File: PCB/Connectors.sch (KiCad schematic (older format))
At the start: 16 parts, among them J1 S2B-PH-SM4-TB, J10 DNP, J11 DNP, J12 DNP, J13 DNP, J2 TRANSDUCER, J3 DNP, J4 PH1-08-UA, J5 DNP, J6 DNP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

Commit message: Rearrange FPGA connections, combine VGA and ADC debug headers, layout most of VGA and ADC circuits
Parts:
- removed J10: DNP, Pin_Headers:Pin_Header_Straight_1x05_Pitch2.54mm, symbol Connector:Conn_01x05_Male
- removed J8: DNP, Pin_Headers:Pin_Header_Straight_1x03_Pitch2.54mm, symbol Connector:Conn_01x03_Male
- added J8: PH1-08-UA, Pin_Headers:Pin_Header_Straight_1x08_Pitch2.54mm, symbol Connector:Conn_01x08_Male
- renumbered J11 to J10, J12 to J11, J13 to J12
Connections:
- net ADC-SCK: now also J8.6 (Pin_6)
- net ADC-SDO: now also J8.7 (Pin_7)
- net ADC-~CS: now also J8.8 (Pin_8)
- net VGA-D0: now also J8.2 (Pin_2)
- net VGA-D1: now also J8.5 (Pin_5)
- net VGA-SCK: now also J8.3 (Pin_3)
- net VGA-~CS0: now also J8.1 (Pin_1)
- net VGA-~CS1: now also J8.4 (Pin_4)
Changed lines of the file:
@@
 	1    0    0    -1
-$EndComp
-$Comp
-L Connector:Conn_01x08_Male J4
-U 1 1 5DD08B5F
-P 3000 4200
-F 0 "J4" H 2972 4174 50  0000 R CNN
-F 1 "PH1-08-UA" H 2972 4083 50  0000 R CNN
-F 2 "Pin_Headers:Pin_Header_Straight_1x08_Pitch2.54mm" H 3000 4200 50  0001 C CNN
-F 3 "https://www.digikey.ca/product-detail/en/adam-tech/PH1-08-UA/2057-PH1-08-UA-ND/9830442" H 3000 4200 50  0001 C CNN
-	1    3000 4200
-	-1   0    0    -1
 $EndComp
 Text GLabel 2750 4000 0    50   Input ~ 0
@@
 $EndComp
 $Comp
-L Connector:Conn_01x02_Male J12
+L Connector:Conn_01x02_Male J11
 U 1 1 5DED5F02
 P 6500 5950
-F 0 "J12" H 6472 5832 50  0000 R CNN
+F 0 "J11" H 6472 5832 50  0000 R CNN
 F 1 "DNP" H 6472 5923 50  0000 R CNN
 F 2 "Pin_Headers:Pin_Header_Straight_1x02_Pitch2.54mm" H 6500 5950 50  0001 C CNN
@@
 Text GLabel 8800 4900 0    50   Input ~ 0
 ADC-SDO
-Text GLabel 8800 5600 0    50   Input ~ 0
+Text GLabel 8800 5500 0    50   Input ~ 0
 VGA-~CS0
-Text GLabel 8800 5500 0    50   Input ~ 0
+Text GLabel 8800 5400 0    50   Input ~ 0
 VGA-D0
-Text GLabel 8800 5400 0    50   Input ~ 0
+Text GLabel 8800 5300 0    50   Input ~ 0
 VGA-SCK
+Text GLabel 8800 5100 0    50   Input ~ 0
+VGA-D1
 Text GLabel 8800 5200 0    50   Input ~ 0
-VGA-D1
-Text GLabel 8800 5300 0    50   Input ~ 0
 VGA-~CS1
 Text GLabel 8800 6100 0    50   Input ~ 0
@@
 Wire Wire Line
 	8800 4600 8850 4600
-$Comp
-L Connector:Conn_01x03_Male J8
-U 1 1 5E22DC4D
-P 9050 4900
-F 0 "J8" H 9022 4832 50  0000 R CNN
-F 1 "DNP" H 9022 4923 50  0000 R CNN
-F 2 "Pin_Headers:Pin_Header_Straight_1x03_Pitch2.54mm" H 9050 4900 50  0001 C CNN
-F 3 "~" H 9050 4900 50  0001 C CNN
-	1    9050 4900
-	-1   0    0    1
-$EndComp
 Wire Wire Line
 	8800 4800 8850 4800
@@
 	8800 5000 8850 5000
 Wire Wire Line
+	8800 5100 8850 5100
+Wire Wire Line
 	8800 5200 8850 5200
 Wire Wire Line
@@
 	8800 5400 8850 5400
 Wire Wire Line
-	8800 5500 8850 5500
-Wire Wire Line
-	8850 5600 8800 5600
+	8850 5500 8800 5500
 Wire Wire Line
 	8800 5800 8850 5800
@@
 $EndComp
 $Comp
-L Connector_Generic:Conn_02x05_Odd_Even J11
+L Connector_Generic:Conn_02x05_Odd_Even J10
 U 1 1 5E09FA0E
 P 2750 5750
-F 0 "J11" H 2800 6167 50  0000 C CNN
+F 0 "J10" H 2800 6167 50  0000 C CNN
 F 1 "DNP" H 2800 6076 50  0000 C CNN
 F 2 "Pin_Headers:Pin_Header_Straight_2x05_Pitch2.54mm" H 2750 5750 50  0001 C CNN
@@
 NoConn ~ 2550 5850
 $Comp
-L Connector:Conn_01x04_Male J13
+L Connector:Conn_01x04_Male J12
 U 1 1 5E5FD68B
 P 9050 6000
-F 0 "J13" H 9022 5882 50  0000 R CNN
+F 0 "J12" H 9022 5882 50  0000 R CNN
 F 1 "DNP" H 9022 5973 50  0000 R CNN
 F 2 "Pin_Headers:Pin_Header_Straight_1x04_Pitch2.54mm" H 9050 6000 50  0001 C CNN
 F 3 "~" H 9050 6000 50  0001 C CNN
 	1    9050 6000
-	-1   0    0    1
-$EndComp
-$Comp
-L Connector:Conn_01x05_Male J10
-U 1 1 5E600171
-P 9050 5400
-F 0 "J10" H 9022 5332 50  0000 R CNN
-F 1 "DNP" H 9022 5423 50  0000 R CNN
-F 2 "Pin_Headers:Pin_Header_Straight_1x05_Pitch2.54mm" H 9050 5400 50  0001 C CNN
-F 3 "~" H 9050 5400 50  0001 C CNN
-	1    9050 5400
 	-1   0    0    1
 $EndComp
@@
 	-1   0    0    -1
 $EndComp
+$Comp
+L Connector:Conn_01x08_Male J4
+U 1 1 5DD08B5F
+P 3000 4200
+F 0 "J4" H 2972 4174 50  0000 R CNN
+F 1 "PH1-08-UA" H 2972 4083 50  0000 R CNN
+F 2 "Pin_Headers:Pin_Header_Straight_1x08_Pitch2.54mm" H 3000 4200 50  0001 C CNN
+F 3 "https://www.digikey.ca/product-detail/en/adam-tech/PH1-08-UA/2057-PH1-08-UA-ND/9830442" H 3000 4200 50  0001 C CNN
+	1    3000 4200
+	-1   0    0    -1
+$EndComp
+$Comp
+L Connector:Conn_01x08_Male J8
+U 1 1 5E2E1494
+P 9050 5200
+F 0 "J8" H 9022 5174 50  0000 R CNN
+F 1 "PH1-08-UA" H 9022 5083 50  0000 R CNN
+F 2 "Pin_Headers:Pin_Header_Straight_1x08_Pitch2.54mm" H 9050 5200 50  0001 C CNN
+F 3 "https://www.digikey.ca/product-detail/en/adam-tech/PH1-08-UA/2057-PH1-08-UA-ND/9830442" H 9050 5200 50  0001 C CNN
+	1    9050 5200
+	-1   0    0    1
+$EndComp
 $EndSCHEMATC

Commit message: Add additional mounting holes, optimize receive power supply connections for layout, simplify FPGA analog ground, layout 3v3 and 1v2 supplies
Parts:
- added H3, H4: MountingHole_Pad, Mounting_Holes:MountingHole_4mm_Pad_Via, symbol Mechanical:MountingHole_Pad
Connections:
- net GND: now also H3.1, H4.1
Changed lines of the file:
@@
 $EndDescr
 $Comp
-L power:GND #PWR0179
+L power:GND #PWR0178
 U 1 1 5DCE40E5
 P 2750 2200
-F 0 "#PWR0179" H 2750 1950 50  0001 C CNN
+F 0 "#PWR0178" H 2750 1950 50  0001 C CNN
 F 1 "GND" H 2755 2027 50  0000 C CNN
 F 2 "" H 2750 2200 50  0001 C CNN
@@
 $EndComp
 $Comp
-L power:+BATT #PWR0177
+L power:+BATT #PWR0176
 U 1 1 5DCED91D
 P 3000 2000
-F 0 "#PWR0177" H 3000 1850 50  0001 C CNN
+F 0 "#PWR0176" H 3000 1850 50  0001 C CNN
 F 1 "+BATT" H 3015 2173 50  0000 C CNN
 F 2 "" H 3000 2000 50  0001 C CNN
@@
 	5700 2550 5700 2650
 $Comp
-L power:GND #PWR0181
+L power:GND #PWR0182
 U 1 1 5DE80E0C
 P 5700 3050
-F 0 "#PWR0181" H 5700 2800 50  0001 C CNN
+F 0 "#PWR0182" H 5700 2800 50  0001 C CNN
 F 1 "GND" H 5705 2877 50  0000 C CNN
 F 2 "" H 5700 3050 50  0001 C CNN
@@
 FPGA-TDO
 $Comp
-L power:+3V3 #PWR0182
+L power:+3V3 #PWR0183
 U 1 1 5DED008E
 P 2700 3900
-F 0 "#PWR0182" H 2700 3750 50  0001 C CNN
+F 0 "#PWR0183" H 2700 3750 50  0001 C CNN
 F 1 "+3V3" H 2715 4073 50  0000 C CNN
 F 2 "" H 2700 3900 50  0001 C CNN
@@
 	2800 4600 2750 4600
 $Comp
-L power:GND #PWR0185
+L power:GND #PWR0186
 U 1 1 5DD2AB1C
 P 2050 4450
-F 0 "#PWR0185" H 2050 4200 50  0001 C CNN
+F 0 "#PWR0186" H 2050 4200 50  0001 C CNN
 F 1 "GND" H 2055 4277 50  0000 C CNN
 F 2 "" H 2050 4450 50  0001 C CNN
@@
 Connection ~ 2050 4400
 $Comp
-L power:GND #PWR0193
+L power:GND #PWR0194
 U 1 1 5DD3A2BB
 P 3150 6000
-F 0 "#PWR0193" H 3150 5750 50  0001 C CNN
+F 0 "#PWR0194" H 3150 5750 50  0001 C CNN
 F 1 "GND" H 3155 5827 50  0000 C CNN
 F 2 "" H 3150 6000 50  0001 C CNN
@@
 	5950 2650 5950 3000
 $Comp
-L power:+2V5 #PWR0190
+L power:+2V5 #PWR0191
 U 1 1 5DDAEE31
 P 3250 5650
-F 0 "#PWR0190" H 3250 5500 50  0001 C CNN
+F 0 "#PWR0191" H 3250 5500 50  0001 C CNN
 F 1 "+2V5" H 3265 5823 50  0000 C CNN
 F 2 "" H 3250 5650 50  0001 C CNN
@@
 $EndComp
 $Comp
-L power:+1V2 #PWR0183
+L power:+1V2 #PWR0184
 U 1 1 5DECE3B1
 P 6200 3900
-F 0 "#PWR0183" H 6200 3750 50  0001 C CNN
+F 0 "#PWR0184" H 6200 3750 50  0001 C CNN
 F 1 "+1V2" H 6215 4073 50  0000 C CNN
 F 2 "" H 6200 3900 50  0001 C CNN
@@
 	6200 3900 6300 3900
 $Comp
-L power:GND #PWR0184
+L power:GND #PWR0185
 U 1 1 5DECF8CC
 P 6200 4000
-F 0 "#PWR0184" H 6200 3750 50  0001 C CNN
+F 0 "#PWR0185" H 6200 3750 50  0001 C CNN
 F 1 "GND" H 6205 3827 50  0000 C CNN
 F 2 "" H 6200 4000 50  0001 C CNN
@@
 	6200 5200 6300 5200
 $Comp
-L power:GND #PWR0189
+L power:GND #PWR0190
 U 1 1 5DED29DD
 P 6200 5300
-F 0 "#PWR0189" H 6200 5050 50  0001 C CNN
+F 0 "#PWR0190" H 6200 5050 50  0001 C CNN
 F 1 "GND" H 6205 5127 50  0000 C CNN
 F 2 "" H 6200 5300 50  0001 C CNN
@@
 	6200 5300 6300 5300
 $Comp
-L power:+12V #PWR0188
+L power:+12V #PWR0189
 U 1 1 5DED51C9
 P 6200 5200
-F 0 "#PWR0188" H 6200 5050 50  0001 C CNN
+F 0 "#PWR0189" H 6200 5050 50  0001 C CNN
 F 1 "+12V" H 6215 5373 50  0000 C CNN
 F 2 "" H 6200 5200 50  0001 C CNN
@@
 	6200 5850 6300 5850
 $Comp
-L power:GND #PWR0192
+L power:GND #PWR0193
 U 1 1 5DED5F0D
 P 6200 5950
-F 0 "#PWR0192" H 6200 5700 50  0001 C CNN
+F 0 "#PWR0193" H 6200 5700 50  0001 C CNN
 F 1 "GND" H 6205 5777 50  0000 C CNN
 F 2 "" H 6200 5950 50  0001 C CNN
@@
 	6200 5950 6300 5950
 $Comp
-L Parts:+50V #PWR0191
+L Parts:+50V #PWR0192
 U 1 1 5DED7ED3
 P 6200 5850
-F 0 "#PWR0191" H 6200 5700 50  0001 C CNN
+F 0 "#PWR0192" H 6200 5700 50  0001 C CNN
 F 1 "+50V" H 6215 6023 50  0000 C CNN
 F 2 "" H 6200 5850 50  0001 C CNN
@@
 $EndComp
 $Comp
-L power:GND #PWR0187
+L power:GND #PWR0188
 U 1 1 5DEFAC45
 P 6200 4650
-F 0 "#PWR0187" H 6200 4400 50  0001 C CNN
+F 0 "#PWR0188" H 6200 4400 50  0001 C CNN
 F 1 "GND" H 6205 4477 50  0000 C CNN
 F 2 "" H 6200 4650 50  0001 C CNN
@@
 $EndComp
 $Comp
-L power:GND #PWR0180
+L power:GND #PWR0179
 U 1 1 5E243B36
 P 3550 2250
-F 0 "#PWR0180" H 3550 2000 50  0001 C CNN
+F 0 "#PWR0179" H 3550 2000 50  0001 C CNN
 F 1 "GND" H 3555 2077 50  0000 C CNN
 F 2 "" H 3550 2250 50  0001 C CNN
@@
 $EndComp
 $Comp
-L power:+BATT #PWR0178
+L power:+BATT #PWR0177
 U 1 1 5E24725E
 P 3550 2000
-F 0 "#PWR0178" H 3550 1850 50  0001 C CNN
+F 0 "#PWR0177" H 3550 1850 50  0001 C CNN
 F 1 "+BATT" H 3565 2173 50  0000 C CNN
 F 2 "" H 3550 2000 50  0001 C CNN
@@
 	3550 2000 3650 2000
 $Comp
-L power:+10V #PWR0186
+L power:+10V #PWR0187
 U 1 1 5E281EB9
 P 6200 4550
-F 0 "#PWR0186" H 6200 4400 50  0001 C CNN
+F 0 "#PWR0187" H 6200 4400 50  0001 C CNN
 F 1 "+10V" H 6215 4723 50  0000 C CNN
 F 2 "" H 6200 4550 50  0001 C CNN
@@
 	-1   0    0    1
 $EndComp
+$Comp
+L Mechanical:MountingHole_Pad H3
+U 1 1 5E3FBDE7
+P 3750 2500
+F 0 "H3" V 3704 2650 50  0000 L CNN
+F 1 "MountingHole_Pad" V 3795 2650 50  0000 L CNN
+F 2 "Mounting_Holes:MountingHole_4mm_Pad_Via" H 3750 2500 50  0001 C CNN
+F 3 "~" H 3750 2500 50  0001 C CNN
+	1    3750 2500
+	0    1    1    0
+$EndComp
+$Comp
+L power:GND #PWR0180
+U 1 1 5E3FBDF1
+P 3550 2500
+F 0 "#PWR0180" H 3550 2250 50  0001 C CNN
+F 1 "GND" H 3555 2327 50  0000 C CNN
+F 2 "" H 3550 2500 50  0001 C CNN
+F 3 "" H 3550 2500 50  0001 C CNN
+	1    3550 2500
+	1    0    0    -1
+$EndComp
+Wire Wire Line
+	3550 2500 3650 2500
+$Comp
+L Mechanical:MountingHole_Pad H4
+U 1 1 5E3FEDB8
+P 3750 2750
+F 0 "H4" V 3704 2900 50  0000 L CNN
+F 1 "MountingHole_Pad" V 3795 2900 50  0000 L CNN
+F 2 "Mounting_Holes:MountingHole_4mm_Pad_Via" H 3750 2750 50  0001 C CNN
+F 3 "~" H 3750 2750 50  0001 C CNN
+	1    3750 2750
+	0    1    1    0
+$EndComp
+$Comp
+L power:GND #PWR0181
+U 1 1 5E3FEDC2
+P 3550 2750
+F 0 "#PWR0181" H 3550 2500 50  0001 C CNN
+F 1 "GND" H 3555 2577 50  0000 C CNN
+F 2 "" H 3550 2750 50  0001 C CNN
+F 3 "" H 3550 2750 50  0001 C CNN
+	1    3550 2750
+	1    0    0    -1
+$EndComp
+Wire Wire Line
+	3550 2750 3650 2750
 $EndSCHEMATC

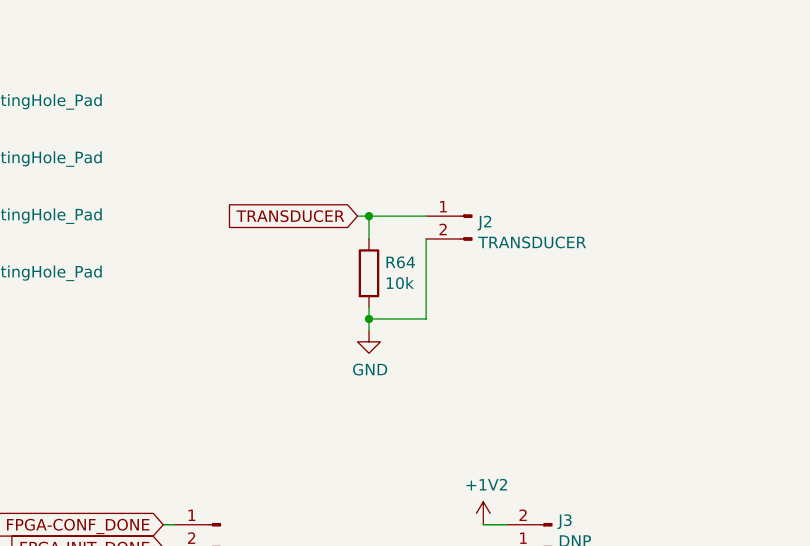
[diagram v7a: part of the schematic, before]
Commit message: Adjust receive circuit to increase stability (hopefully less likely to oscillate)
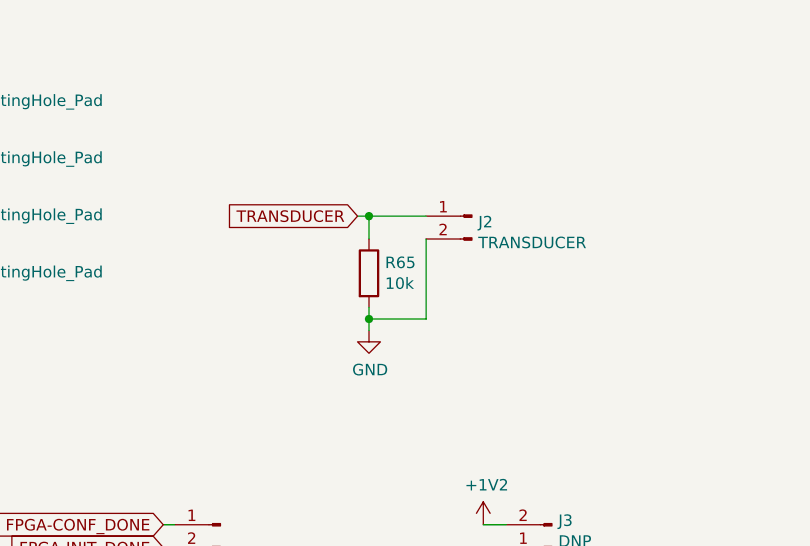
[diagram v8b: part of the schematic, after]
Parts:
- renumbered R64 to R65
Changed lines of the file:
@@
 $EndDescr
 $Comp
-L power:GND #PWR0178
+L power:GND #PWR0182
 U 1 1 5DCE40E5
 P 2750 2200
-F 0 "#PWR0178" H 2750 1950 50  0001 C CNN
+F 0 "#PWR0182" H 2750 1950 50  0001 C CNN
 F 1 "GND" H 2755 2027 50  0000 C CNN
 F 2 "" H 2750 2200 50  0001 C CNN
@@
 $EndComp
 $Comp
-L power:+BATT #PWR0176
+L power:+BATT #PWR0180
 U 1 1 5DCED91D
 P 3000 2000
-F 0 "#PWR0176" H 3000 1850 50  0001 C CNN
+F 0 "#PWR0180" H 3000 1850 50  0001 C CNN
 F 1 "+BATT" H 3015 2173 50  0000 C CNN
 F 2 "" H 3000 2000 50  0001 C CNN
@@
 TRANSDUCER
 $Comp
-L Device:R R64
+L Device:R R65
 U 1 1 5DE80022
 P 5700 2800
-F 0 "R64" H 5770 2846 50  0000 L CNN
+F 0 "R65" H 5770 2846 50  0000 L CNN
 F 1 "10k" H 5770 2755 50  0000 L CNN
 F 2 "Resistors_SMD:R_1206_HandSoldering" V 5630 2800 50  0001 C CNN
@@
 	5700 2550 5700 2650
 $Comp
-L power:GND #PWR0182
+L power:GND #PWR0186
 U 1 1 5DE80E0C
 P 5700 3050
-F 0 "#PWR0182" H 5700 2800 50  0001 C CNN
+F 0 "#PWR0186" H 5700 2800 50  0001 C CNN
 F 1 "GND" H 5705 2877 50  0000 C CNN
 F 2 "" H 5700 3050 50  0001 C CNN
@@
 FPGA-TDO
 $Comp
-L power:+3V3 #PWR0183
+L power:+3V3 #PWR0187
 U 1 1 5DED008E
 P 2700 3900
-F 0 "#PWR0183" H 2700 3750 50  0001 C CNN
+F 0 "#PWR0187" H 2700 3750 50  0001 C CNN
 F 1 "+3V3" H 2715 4073 50  0000 C CNN
 F 2 "" H 2700 3900 50  0001 C CNN
@@
 	2800 4600 2750 4600
 $Comp
-L power:GND #PWR0186
+L power:GND #PWR0190
 U 1 1 5DD2AB1C
 P 2050 4450
-F 0 "#PWR0186" H 2050 4200 50  0001 C CNN
+F 0 "#PWR0190" H 2050 4200 50  0001 C CNN
 F 1 "GND" H 2055 4277 50  0000 C CNN
 F 2 "" H 2050 4450 50  0001 C CNN
@@
 Connection ~ 2050 4400
 $Comp
-L power:GND #PWR0194
+L power:GND #PWR0198
 U 1 1 5DD3A2BB
 P 3150 6000
-F 0 "#PWR0194" H 3150 5750 50  0001 C CNN
+F 0 "#PWR0198" H 3150 5750 50  0001 C CNN
 F 1 "GND" H 3155 5827 50  0000 C CNN
 F 2 "" H 3150 6000 50  0001 C CNN
@@
 	5950 2650 5950 3000
 $Comp
-L power:+2V5 #PWR0191
+L power:+2V5 #PWR0195
 U 1 1 5DDAEE31
 P 3250 5650
-F 0 "#PWR0191" H 3250 5500 50  0001 C CNN
+F 0 "#PWR0195" H 3250 5500 50  0001 C CNN
 F 1 "+2V5" H 3265 5823 50  0000 C CNN
 F 2 "" H 3250 5650 50  0001 C CNN
@@
 $EndComp
 $Comp
-L power:+1V2 #PWR0184
+L power:+1V2 #PWR0188
 U 1 1 5DECE3B1
 P 6200 3900
-F 0 "#PWR0184" H 6200 3750 50  0001 C CNN
+F 0 "#PWR0188" H 6200 3750 50  0001 C CNN
 F 1 "+1V2" H 6215 4073 50  0000 C CNN
 F 2 "" H 6200 3900 50  0001 C CNN
@@
 	6200 3900 6300 3900
 $Comp
-L power:GND #PWR0185
+L power:GND #PWR0189
 U 1 1 5DECF8CC
 P 6200 4000
-F 0 "#PWR0185" H 6200 3750 50  0001 C CNN
+F 0 "#PWR0189" H 6200 3750 50  0001 C CNN
 F 1 "GND" H 6205 3827 50  0000 C CNN
 F 2 "" H 6200 4000 50  0001 C CNN
@@
 	6200 5200 6300 5200
 $Comp
-L power:GND #PWR0190
+L power:GND #PWR0194
 U 1 1 5DED29DD
 P 6200 5300
-F 0 "#PWR0190" H 6200 5050 50  0001 C CNN
+F 0 "#PWR0194" H 6200 5050 50  0001 C CNN
 F 1 "GND" H 6205 5127 50  0000 C CNN
 F 2 "" H 6200 5300 50  0001 C CNN
@@
 	6200 5300 6300 5300
 $Comp
-L power:+12V #PWR0189
+L power:+12V #PWR0193
 U 1 1 5DED51C9
 P 6200 5200
-F 0 "#PWR0189" H 6200 5050 50  0001 C CNN
+F 0 "#PWR0193" H 6200 5050 50  0001 C CNN
 F 1 "+12V" H 6215 5373 50  0000 C CNN
 F 2 "" H 6200 5200 50  0001 C CNN
@@
 	6200 5850 6300 5850
 $Comp
-L power:GND #PWR0193
+L power:GND #PWR0197
 U 1 1 5DED5F0D
 P 6200 5950
-F 0 "#PWR0193" H 6200 5700 50  0001 C CNN
+F 0 "#PWR0197" H 6200 5700 50  0001 C CNN
 F 1 "GND" H 6205 5777 50  0000 C CNN
 F 2 "" H 6200 5950 50  0001 C CNN
@@
 	6200 5950 6300 5950
 $Comp
-L Parts:+50V #PWR0192
+L Parts:+50V #PWR0196
 U 1 1 5DED7ED3
 P 6200 5850
-F 0 "#PWR0192" H 6200 5700 50  0001 C CNN
+F 0 "#PWR0196" H 6200 5700 50  0001 C CNN
 F 1 "+50V" H 6215 6023 50  0000 C CNN
 F 2 "" H 6200 5850 50  0001 C CNN
@@
 $EndComp
 $Comp
-L power:GND #PWR0188
+L power:GND #PWR0192
 U 1 1 5DEFAC45
 P 6200 4650
-F 0 "#PWR0188" H 6200 4400 50  0001 C CNN
+F 0 "#PWR0192" H 6200 4400 50  0001 C CNN
 F 1 "GND" H 6205 4477 50  0000 C CNN
 F 2 "" H 6200 4650 50  0001 C CNN
@@
 $EndComp
 $Comp
-L power:GND #PWR0179
+L power:GND #PWR0183
 U 1 1 5E243B36
 P 3550 2250
-F 0 "#PWR0179" H 3550 2000 50  0001 C CNN
+F 0 "#PWR0183" H 3550 2000 50  0001 C CNN
 F 1 "GND" H 3555 2077 50  0000 C CNN
 F 2 "" H 3550 2250 50  0001 C CNN
@@
 $EndComp
 $Comp
-L power:+BATT #PWR0177
+L power:+BATT #PWR0181
 U 1 1 5E24725E
 P 3550 2000
-F 0 "#PWR0177" H 3550 1850 50  0001 C CNN
+F 0 "#PWR0181" H 3550 1850 50  0001 C CNN
 F 1 "+BATT" H 3565 2173 50  0000 C CNN
 F 2 "" H 3550 2000 50  0001 C CNN
@@
 	3550 2000 3650 2000
 $Comp
-L power:+10V #PWR0187
+L power:+10V #PWR0191
 U 1 1 5E281EB9
 P 6200 4550
-F 0 "#PWR0187" H 6200 4400 50  0001 C CNN
+F 0 "#PWR0191" H 6200 4400 50  0001 C CNN
 F 1 "+10V" H 6215 4723 50  0000 C CNN
 F 2 "" H 6200 4550 50  0001 C CNN
@@
 $EndComp
 $Comp
-L power:GND #PWR0180
+L power:GND #PWR0184
 U 1 1 5E3FBDF1
 P 3550 2500
-F 0 "#PWR0180" H 3550 2250 50  0001 C CNN
+F 0 "#PWR0184" H 3550 2250 50  0001 C CNN
 F 1 "GND" H 3555 2327 50  0000 C CNN
 F 2 "" H 3550 2500 50  0001 C CNN
@@
 $EndComp
 $Comp
-L power:GND #PWR0181
+L power:GND #PWR0185
 U 1 1 5E3FEDC2
 P 3550 2750
-F 0 "#PWR0181" H 3550 2500 50  0001 C CNN
+F 0 "#PWR0185" H 3550 2500 50  0001 C CNN
 F 1 "GND" H 3555 2577 50  0000 C CNN
 F 2 "" H 3550 2750 50  0001 C CNN
